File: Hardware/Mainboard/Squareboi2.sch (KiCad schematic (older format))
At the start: 24 parts, among them J1 GB-CART, J10 TP_CLK, J11 TP_40, J12 TP_RST, J2 ROMC_L, J4 ROMC_C, J5 RAMC_L, J6 RAMC_R, J7 JTAG, J8 AUX_POW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

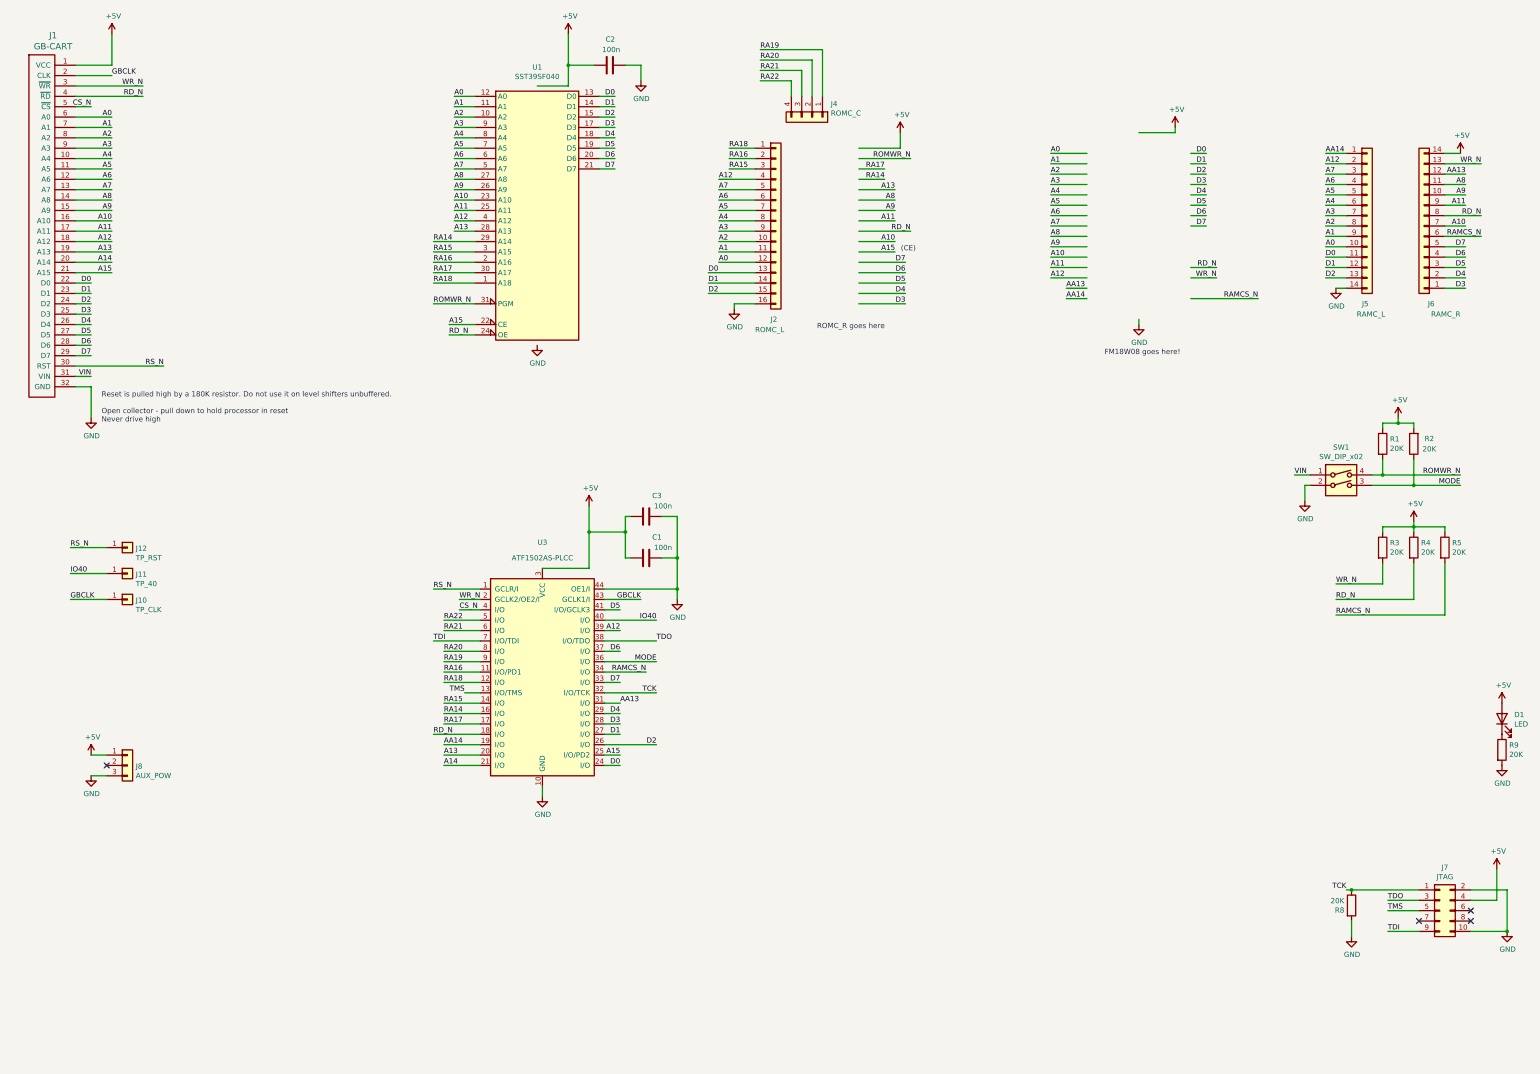
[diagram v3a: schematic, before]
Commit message: Reorganize schematic
Divide schematic into functional blocks, clean up comments
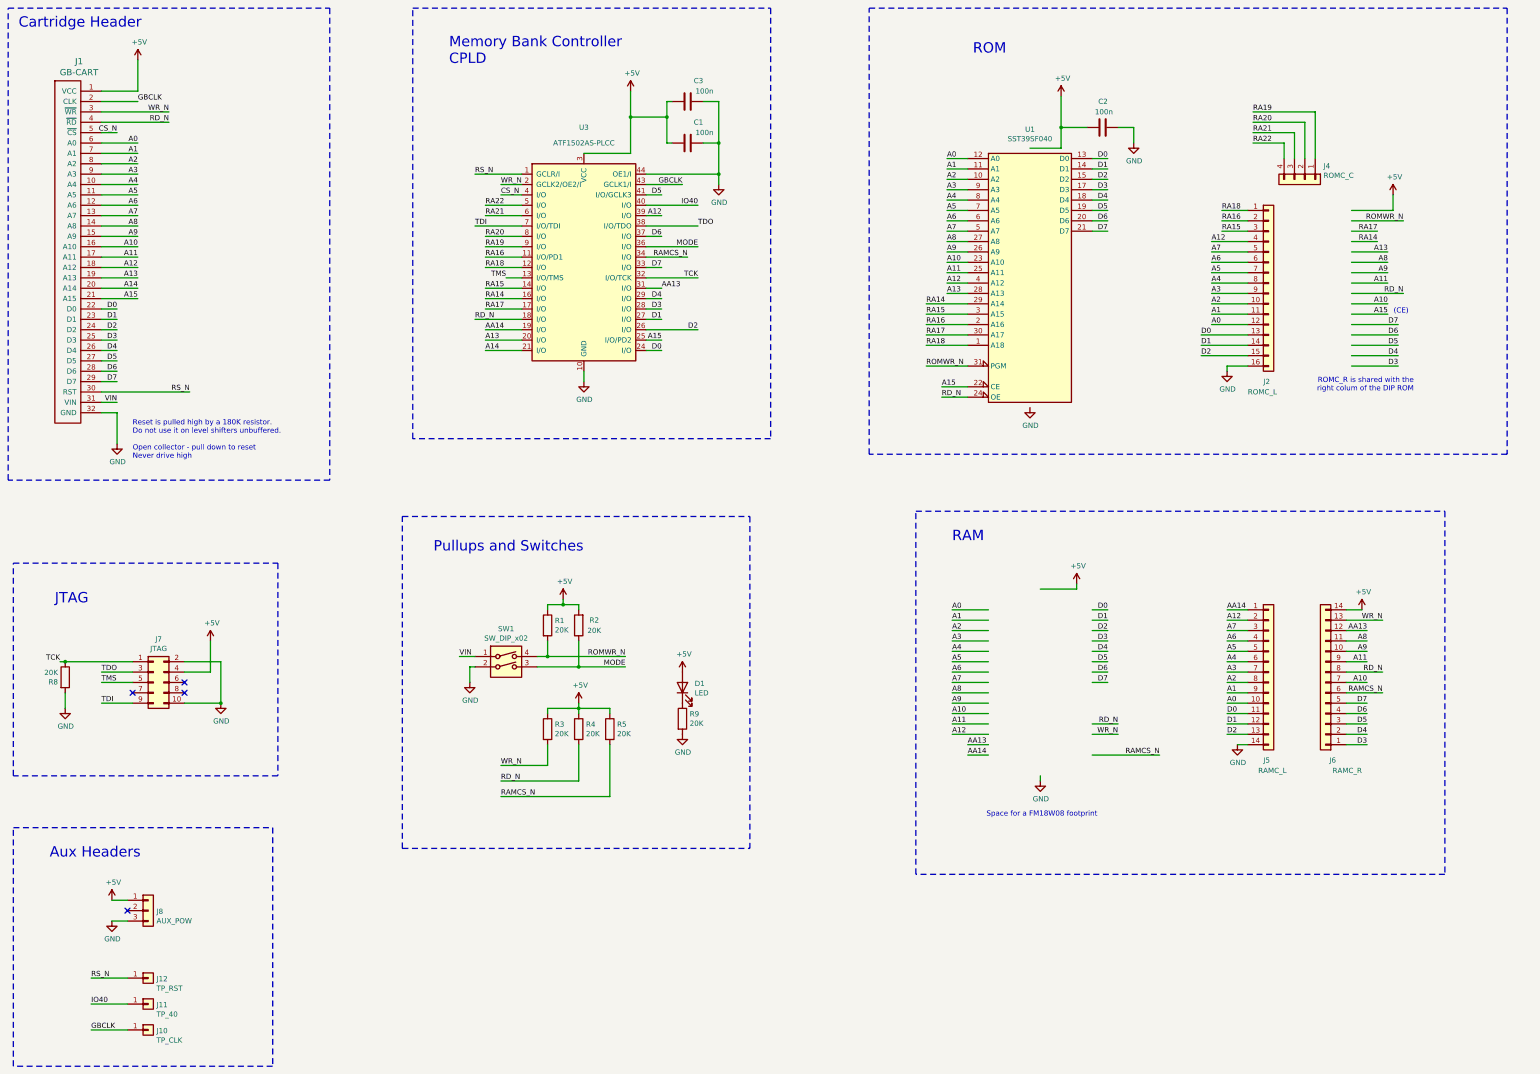
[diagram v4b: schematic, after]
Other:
- note added: "Aux Headers"
- note added: "Cartridge Header"
- note added: "JTAG"
- note added: "Memory Bank Controller\nCPLD"
- note added: "Pullups and Switches"
- note added: "RAM"
- note added: "ROM"
- note added: "ROMC_R is shared with the\n right colum of the DIP ROM"
- note added: "Reset is pulled high by a 180K resistor. \nDo not use it on level shifters unbuffered.\n\nOpen collector - pull down to reset\nNever drive high"
- note added: "Space for a FM18W08 footprint"
- note removed: "FM18W08 goes here!"
- note removed: "ROMC_R goes here"
- note removed: "Reset is pulled high by a 180K resistor. Do not use it on level shifters unbuffered.\n\nOpen collector - pull down to hold processor in reset\nNever drive high"
- moved on the sheet: C1, C2, C3, D1, J1, J10, J11, J12, J2, J4, J5, J6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
